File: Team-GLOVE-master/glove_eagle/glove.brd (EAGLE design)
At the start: 63.5 x 38.1 mm, 51 parts, among them J1 MICRO_USB_B_JST_MC5BR3-M404-4S, U1 BNO055, U3 NRF51822QF, U4 MCP73831, X3 ABS05-32.768KHZ-9-T

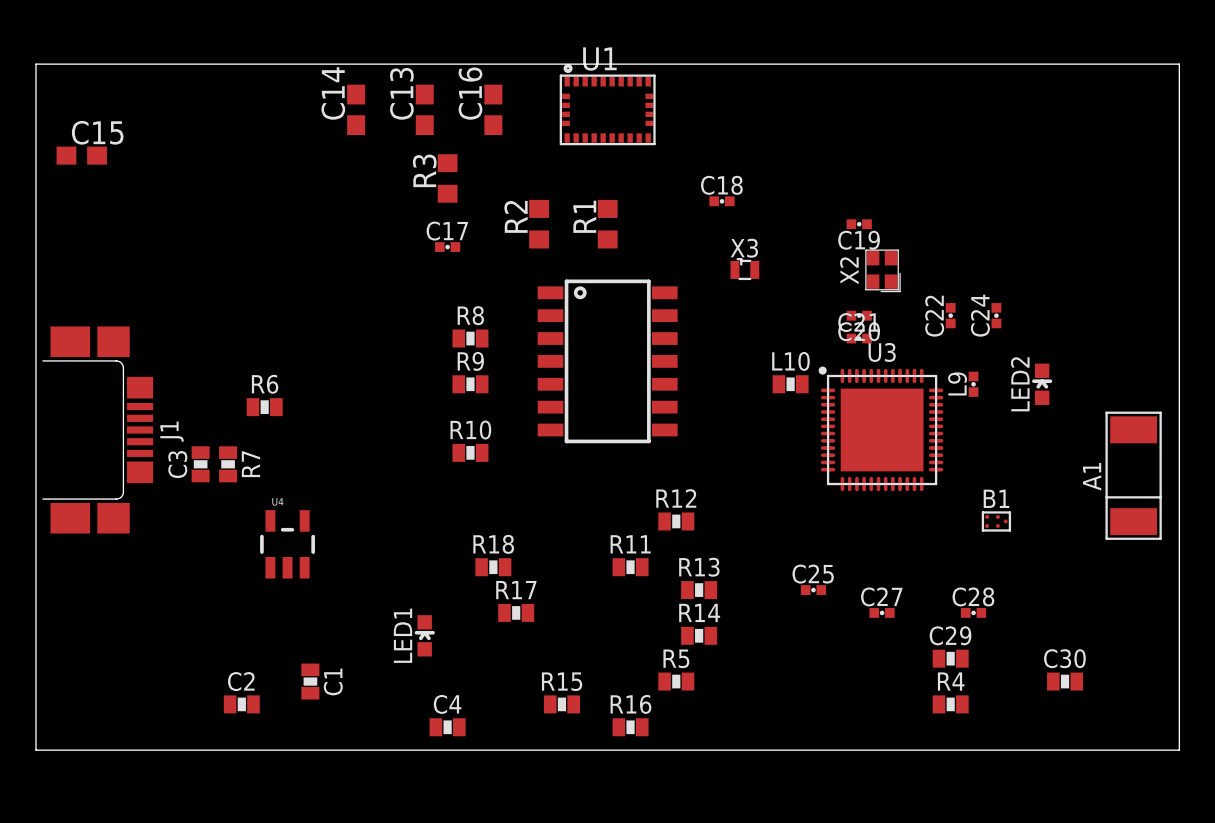
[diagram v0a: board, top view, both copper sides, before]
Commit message: Finished routing nearly completed board
Still lots of modifications to make, but it's a start.
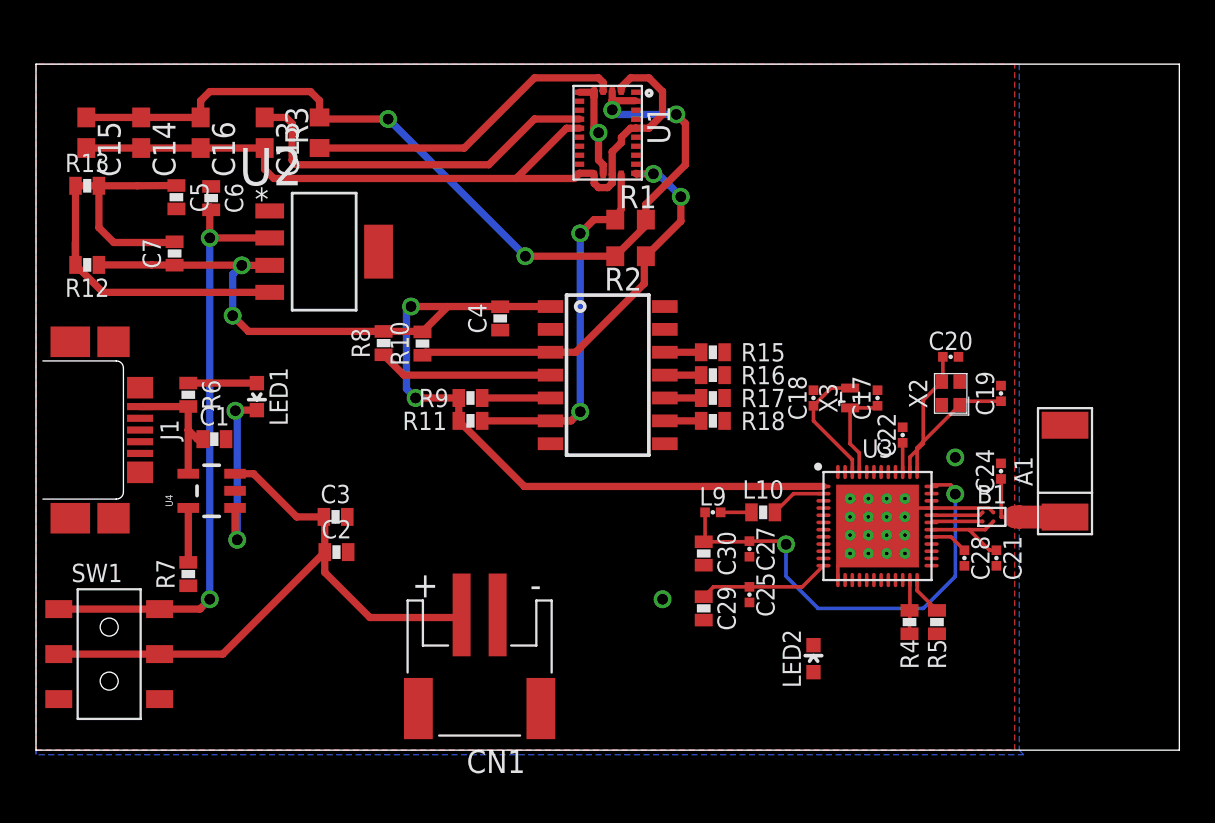
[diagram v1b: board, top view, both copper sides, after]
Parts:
- removed R14: (no value), passives:0603-RES
- added C5: (no value), passives:0603_CAP
- added C6, C7: 10 uF, passives:0603_CAP
- added CN1: (no value), adafruit:JST-PH-2-SMT-RA
- added SW1: (no value), adafruit:EG1390
- added U2: LP3855EMP-ADJ, LP3855EMP-ADJ:SOT150P696X180-5N
- R15, R16, R17, R18: value (none) -> 10 k
- R9: value (none) -> 47 k
- moved R13 40.7 mm to (2.84, 31.3)
- moved R12 35.7 mm to (2.84, 26.9), turned to 180 degrees
- moved C17 25.3 mm to (46.7, 19.6), turned to 90 degrees
- moved C4 22.9 mm to (25.8, 24.0), turned to 270 degrees
- moved C30 21.3 mm to (37.1, 10.9), turned to 270 degrees
- moved R15 21.3 mm to (37.6, 22.1), turned to 180 degrees
- moved R16 20.1 mm to (37.6, 20.8), turned to 180 degrees
- moved LED2 19.8 mm to (43.2, 5.08)
- moved C16 16.3 mm to (9.14, 34.3), turned to 270 degrees
- moved LED1 16.2 mm to (12.3, 19.6), turned to 180 degrees
- moved R17 16.2 mm to (37.6, 19.6), turned to 180 degrees
- moved L9 16.1 mm to (37.6, 13.2), turned to 0 degrees
- moved R5 14.8 mm to (50.0, 7.11), turned to 90 degrees
- moved R18 14.7 mm to (37.6, 18.3), turned to 180 degrees
- moved C1 14.5 mm to (9.91, 17.3), turned to 0 degrees
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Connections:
- removed net N$10: R13.1
- removed net N$11: R14.2, U$1.P$9
- removed net N$13: R14.1
- removed net N$6: R12.2, U$1.P$7
- removed net N$8: R13.2, U$1.P$8
- new net N$5: C6.2, SW1.O1, SW1.O2, U2.2
- net GND: now also C6.1, C7.2, CN1.2, R13.2, U2.5
- net N$1: now also CN1.1, SW1.P1, SW1.P2
- net N$7: now also C5.1, R12.2, R13.1, U2.4; no longer R12.1
- net VCC: now also C7.1, R12.1, U2.3
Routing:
- net VCC: track 0.00 -> 71.4 mm, vias 0 -> 4
- net VDD: track 0.00 -> 50.6 mm, vias 0 -> 4
- net GNDIO: track 0.00 -> 46.0 mm
- net GND: track 0.00 -> 38.9 mm, vias 0 -> 19
- net N$1: track 0.00 -> 34.8 mm
- net N$5: track 0.00 -> 33.9 mm, vias 0 -> 2
- net N$16: track 0.00 -> 25.7 mm, vias 0 -> 2
- net SDA: track 0.00 -> 22.7 mm, vias 0 -> 2
- net N$7: track 0.00 -> 22.7 mm
- net N$9: track 0.00 -> 20.8 mm
- net SCL: track 0.00 -> 20.7 mm, vias 0 -> 2
- net N$18: track 0.00 -> 18.0 mm
- net N$3: track 0.00 -> 10.4 mm, vias 0 -> 2
- net N$40: track 0.00 -> 9.74 mm
- net N$38: track 0.00 -> 7.44 mm
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- added copper zone on layer 1, net GND
- added copper zone on layer 16, net GND
